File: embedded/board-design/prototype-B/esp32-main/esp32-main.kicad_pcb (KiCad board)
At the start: 2 copper layers, 75 x 135.5 mm, 84 parts, among them J1 Conn_ARM_JTAG_SWD_10, J2 Conn_01x08_Socket, J3 Conn_01x08_Socket, J4 0473460001, J5 Conn_01x02_Socket, J6 Conn_01x03_Socket, J7 Conn_01x02_Socket, J8 Conn_01x03_Socket, Q1 BC817, Q2 BC817, Q3 FDN340P, Q4 FDN340P, Q5 BC807, Q6 FDN340P, Q7 FDN340P, U1 ESP32-WROVER-E, U2 BD48ExxG, U3 FT231XS, U4 TPS61090, U5 LTC4054ES5-4.2

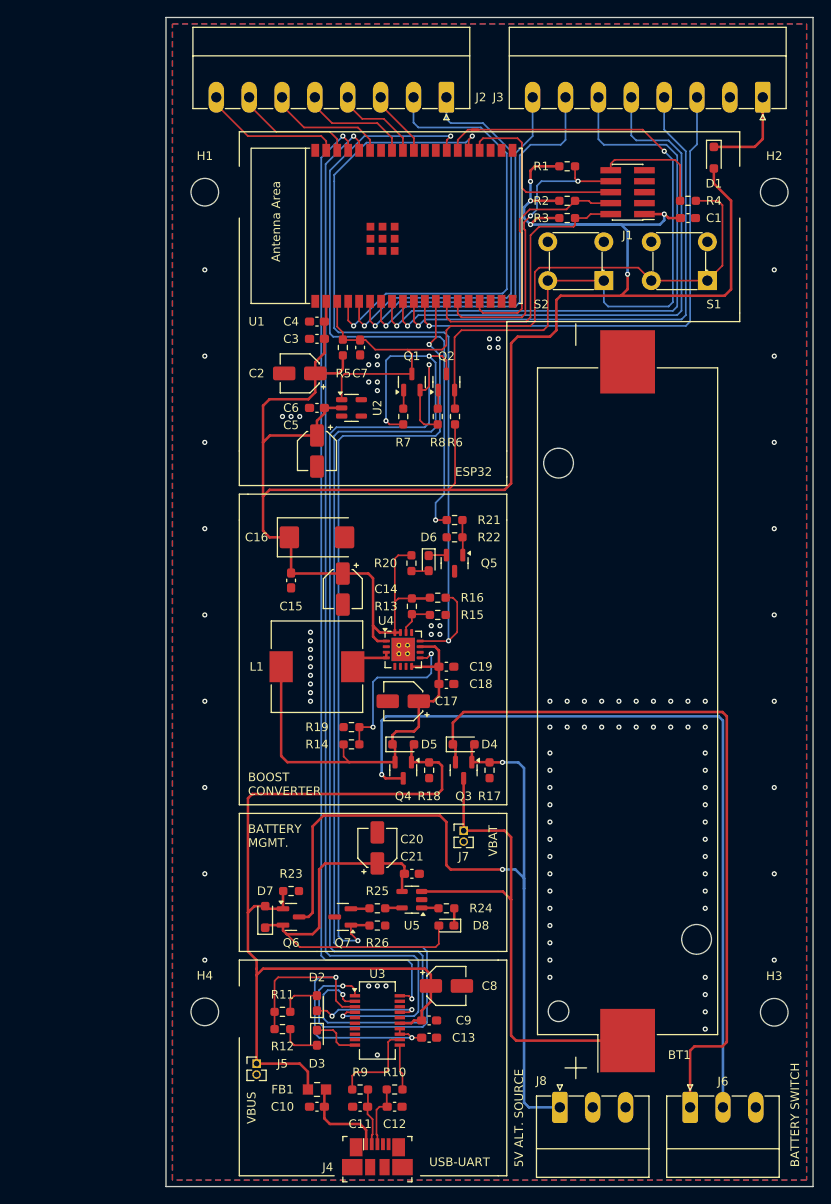
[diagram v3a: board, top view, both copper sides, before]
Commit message: [prototype-B]
Refactored hardware implementation. Reduced board size.

Signed-off-by: Nicolae-Andrei Vasile <vasilenicolaeandrei@gmail.com>
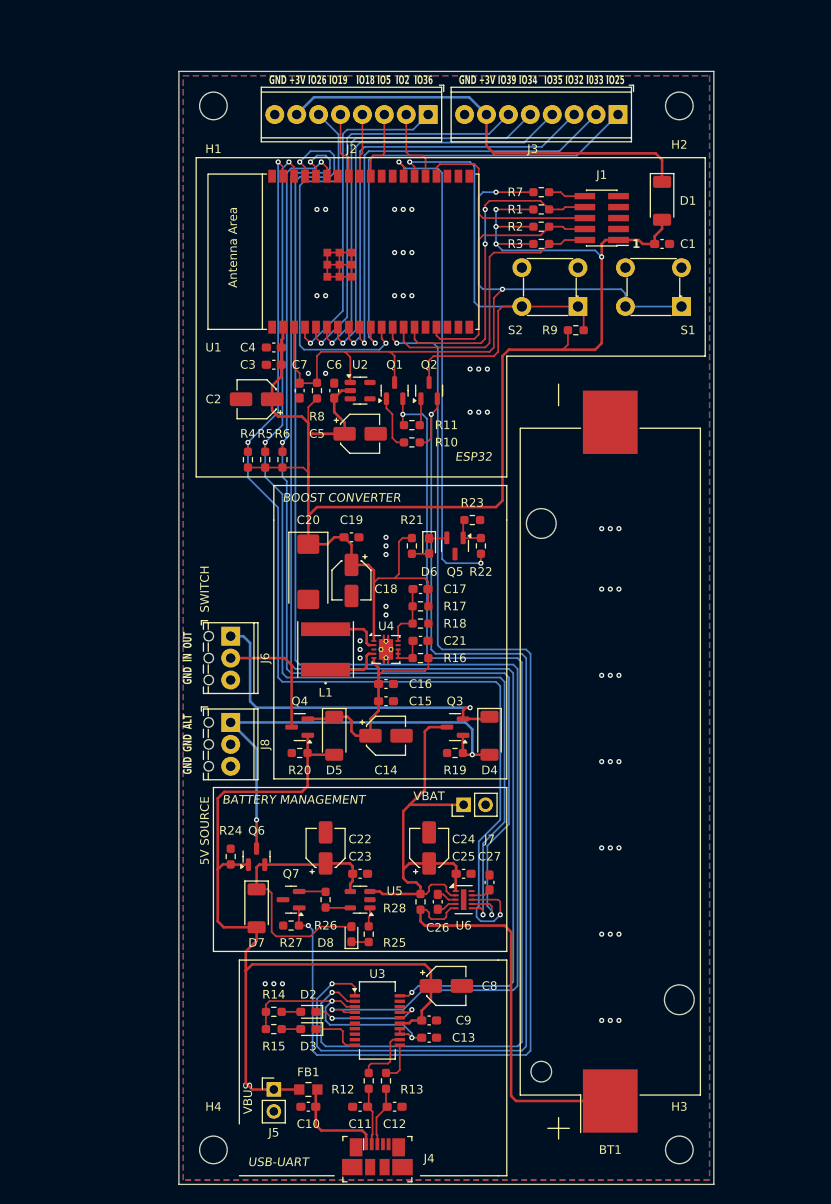
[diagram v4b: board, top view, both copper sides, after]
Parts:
- removed the R26 at (132.0, 126.0)
- added C22: 10uF/16V/20%/4x3mm, Capacitor_SMD:CP_Elec_4x3, F.Cu at (126.0, 117.0)
- added C23: 100nF/6.3V/20%/C0603, Capacitor_SMD:C_0603_1608Metric_Pad1.08x0.95mm_HandSolder, F.Cu at (130.0, 120.0)
- added C24: 10uF/16V/20%/4x3mm, Capacitor_SMD:CP_Elec_4x3, F.Cu at (138.0, 117.0)
- added C25: 100nF/6.3V/20%/C0603, Capacitor_SMD:C_0603_1608Metric_Pad1.08x0.95mm_HandSolder, F.Cu at (142.0, 120.0)
- added C26: 470nF/6.3V/20%/C0603, Capacitor_SMD:C_0603_1608Metric_Pad1.08x0.95mm_HandSolder, F.Cu at (139.0, 123.2)
- added C27: 1uF/6.3V/20%/C0603, Capacitor_SMD:C_0603_1608Metric_Pad1.08x0.95mm_HandSolder, F.Cu at (145.0, 121.0)
- added R27: 10K/R0603, Resistor_SMD:R_0603_1608Metric_Pad0.98x0.95mm_HandSolder, F.Cu at (122.0, 126.0)
- added R28: 50m/R0603, Resistor_SMD:R_0603_1608Metric_Pad0.98x0.95mm_HandSolder, F.Cu at (137.0, 123.2)
- added R4: 10K/R0603, Resistor_SMD:R_0603_1608Metric_Pad0.98x0.95mm_HandSolder, F.Cu at (117.0, 72.0)
- added U6: LTC2959, Package_DFN_QFN:DFN-10-1EP_2x3mm_P0.5mm_EP0.64x2.4mm, F.Cu at (142.0, 123.0)
- C16: value 220uF/16V/10%/D/Tantalum -> 100nF/6.3V/20%/C0603; footprint Capacitor_Tantalum_SMD:CP_EIA-7343-31_Kemet-D_Pad2.25x2.55mm_HandSolder -> Capacitor_SMD:C_0603_1608Metric_Pad1.08x0.95mm_HandSolder
- C17: value 22uF/16V/20%/4x3mm -> 2.2pF/6.3V/20%/C0603; footprint Capacitor_SMD:CP_Elec_4x3 -> Capacitor_SMD:C_0603_1608Metric_Pad1.08x0.95mm_HandSolder
- C18: value 10uF/6.3V/20%/C0603 -> 22uF/16V/20%/4x3mm; footprint Capacitor_SMD:C_0603_1608Metric_Pad1.08x0.95mm_HandSolder -> Capacitor_SMD:CP_Elec_4x3
- C19: value 100nF/6.3V/20%/C0603 -> 10uF/6.3V/20%/C0603
- C20: value 10uF/16V/20%/4x3mm -> 220uF/16V/10%/D/Tantalum; footprint Capacitor_SMD:CP_Elec_4x3 -> Capacitor_Tantalum_SMD:CP_EIA-7343-31_Kemet-D_Pad2.25x2.55mm_HandSolder
- D1, D4, D5, D7: value SMD22WS-TP -> PMEG3020EP; footprint Diode_SMD:D_SOD-323_HandSoldering -> Diode_SMD:D_SOD-128
- J2, J3: footprint Connector_Phoenix_MC:PhoenixContact_MC_1,5_8-G-3.81_1x08_P3.81mm_Horizontal -> TerminalBlock_Phoenix:TerminalBlock_Phoenix_MPT-0,5-8-2.54_1x08_P2.54mm_Horizontal
- J5, J7: footprint Connector_PinHeader_1.27mm:PinHeader_1x02_P1.27mm_Vertical -> Connector_PinHeader_2.54mm:PinHeader_1x02_P2.54mm_Vertical
- J6, J8: footprint Connector_Phoenix_MC:PhoenixContact_MC_1,5_3-G-3.81_1x03_P3.81mm_Horizontal -> TerminalBlock_Phoenix:TerminalBlock_Phoenix_MPT-0,5-3-2.54_1x03_P2.54mm_Horizontal
- L1: value CDRH103RNP-8R2NC-B -> NRS6010T1R5MMGF; footprint Inductor_SMD:L_10.4x10.4_H4.8 -> footprints:IND_TAIYO_NRS6010_TAY
- R1, R2, R3: value 100K/R0603 -> 10K/R0603
- R10: renamed from R9; value 27R/R0603 -> 10K/R0603
- R11: renamed from R10; value 27R/R0603 -> 10K/R0603
- R12: renamed from R11; value 270R/R0603 -> 27R/R0603
- R13: renamed from R12; value 270R/R0603 -> 27R/R0603
- R14: renamed from R13; value 1M/R0603 -> 270R/R0603
- R15: renamed from R14; value 2M/R0603 -> 270R/R0603
- R16: renamed from R15; value 180K/R0603 -> 100R/R0603
- R18: renamed from R17; value 100K/R0603 -> 180K/R0603
- R20: renamed from R19; value 390K/R0603 -> 100K/R0603
- R5: renamed from R4; value 0R(board mount) -> 10K/R0603
- R7: renamed from R6; value 10K/R0603 -> 0R(board mount)
- U4: value TPS61090 -> TPS63000; footprint Package_DFN_QFN:Texas_RSA_VQFN-16-1EP_4x4mm_P0.65mm_EP2.7x2.7mm_ThermalVias -> Package_SON:Texas_DRC0010J_ThermalVias
- moved R11 77.0 mm to (136.0, 68.0)
- moved J6 76.3 mm to (115.0, 92.5), turned to -90 degrees
- moved R10 75.2 mm to (136.0, 70.0)
- moved J8 58.7 mm to (115.0, 102.5), turned to -90 degrees
- moved R5 57.5 mm to (119.0, 72.0), turned to -90 degrees
- moved R14 49.6 mm to (120.0, 136.0), turned to 180 degrees
- moved R15 34.2 mm to (120.0, 138.0), turned to 180 degrees
- moved C20 33.0 mm to (124.0, 85.0), turned to -90 degrees
- moved R7 27.9 mm to (151.0, 41.0), turned to 180 degrees
- moved C21 27.0 mm to (137.0, 93.0)
- moved H3 19.4 mm to (167.0, 152.0)
- moved R9 18.9 mm to (155.0, 57.0), turned to 0 degrees
- moved C16 18.8 mm to (133.0, 98.0)
- moved R18 18.8 mm to (137.0, 91.0), turned to 180 degrees
- moved C19 18.6 mm to (129.0, 81.0)
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- renumbered R16 to R17, R18 to R19, R20 to R21, R21 to R22, R22 to R23, R23 to R24, R24 to R25, R25 to R26, R5 to R6, R7 to R8, R8 to R9
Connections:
- net /GPIO18/VSPICLK renamed /GPIO18
- net /GPIO19/VSPIQ renamed /GPIO19
- net /GPIO5/VSPICS0 renamed /GPIO5
- BT1 pad 1: VBAT -> Net-(BT1-+)
- C14 pad 1: +3V3 -> Net-(D5-K)
- C15 pad 1: +3V3 -> Net-(D5-K)
- C16 pad 1: +3V3 -> Net-(D5-K)
- C17 pad 1: Net-(D5-K) -> +3V3
- C17 pad 2: GND -> Net-(U4-FB)
- C18 pad 1: Net-(D5-K) -> +3V3
- C19 pad 1: Net-(D5-K) -> +3V3
- C20 pad 1: Net-(D7-K) -> +3V3
- C21 pad 1: Net-(D7-K) -> Net-(U4-EN)
- J2 pad 1: /GPIO39 -> /GPIO36
- J2 pad 2: /GPIO36 -> /GPIO2
- J2 pad 6: /GPIO21/VSPIHD -> /GPIO26
- J2 pad 7: /GPIO22/VSPIWP -> Net-(D1-K)
- J2 pad 8: /GPIO23/VSPID -> GND
- J3 pad 1: Net-(D1-K) -> /GPIO25
- J3 pad 2: GND -> /GPIO33
- J3 pad 3: /GPIO26 -> /GPIO32
- J3 pad 4: /GPIO25 -> /GPIO35
- J3 pad 5: /GPIO33 -> /GPIO34
- J3 pad 6: /GPIO32 -> /GPIO39
- J3 pad 7: /GPIO35 -> Net-(D1-K)
- J3 pad 8: /GPIO34 -> GND
- L1 pad 1: Net-(D5-K) -> Net-(U4-L1)
- L1 pad 2: Net-(L1-Pad2) -> Net-(U4-L2)
- Q2 pad 2: /BOOT -> /usb-uart/~{DTR}
- Q2 pad 3: /usb-uart/~{DTR} -> /BOOT
- R10 pad 1: Net-(U3-USBDM) -> Net-(Q1-B)
- R10 pad 2: /usb-uart/D- -> /usb-uart/~{DTR}
- R11 pad 1: Net-(U3-USBDP) -> Net-(Q2-B)
- R11 pad 2: /usb-uart/D+ -> /usb-uart/~{RTS}
- R12 pad 1: Net-(D2-A) -> Net-(U3-USBDM)
- R12 pad 2: Net-(U3-3V3OUT) -> /usb-uart/D-
- R13 pad 1: Net-(D3-A) -> Net-(U3-USBDP)
- R13 pad 2: Net-(U3-3V3OUT) -> /usb-uart/D+
- R14 pad 1: +3V3 -> Net-(D2-A)
- R14 pad 2: Net-(U4-FB) -> Net-(U3-3V3OUT)
- R15 pad 1: Net-(D5-K) -> Net-(D3-A)
- R15 pad 2: Net-(U4-LBI) -> Net-(U3-3V3OUT)
- R16 pad 1: Net-(U4-FB) -> Net-(U4-EN)
- R16 pad 2: GND -> Net-(D5-K)
- R17 pad 1: +3V3 -> Net-(U4-FB)
- R17 pad 2: /power-supply/LDO -> +3V3
- R18 pad 2: ALT -> Net-(U4-FB)
- R19 pad 2: VBUS -> ALT
- R20 pad 2: Net-(U4-LBI) -> VBUS
- R5 pad 1: Net-(J1-~{RESET}) -> /battery/SCL
- R5 pad 2: Net-(Q1-C) -> +3V3
- R6 pad 1: +3V3 -> /battery/SDA
- R6 pad 2: Net-(Q1-C) -> +3V3
- R7 pad 1: +3V3 -> Net-(J1-~{RESET})
- R7 pad 2: /BOOT -> Net-(Q1-C)
- R8 pad 1: Net-(Q1-B) -> +3V3
- R8 pad 2: /usb-uart/~{DTR} -> Net-(Q1-C)
- R9 pad 1: Net-(Q2-B) -> +3V3
- R9 pad 2: /usb-uart/~{RTS} -> /BOOT
- U1 pad 24: /power-supply/LDO -> /GPIO2
- U1 pad 33: /GPIO21/VSPIHD -> /battery/SDA
- U1 pad 36: /GPIO22/VSPIWP -> /battery/SCL
- U1 pad 37: /GPIO23/VSPID -> /battery/BAT_INT
- U3 pad 20: /U0TXD -> /U0RXD
- U3 pad 4: /U0RXD -> /U0TXD
- U4 pad 10: GND -> Net-(U4-FB)
- U4 pad 11: Net-(D5-K) -> GND
- U4 pad 2: unconnected-(U4-NC-Pad2) -> Net-(U4-L2)
- U4 pad 3: Net-(L1-Pad2) -> GND
- U4 pad 4: Net-(L1-Pad2) -> Net-(U4-L1)
- U4 pad 5: GND -> Net-(D5-K)
- U4 pad 6: GND -> Net-(U4-EN)
- U4 pad 7: GND -> Net-(U4-EN)
- U4 pad 8: Net-(D5-K) -> Net-(U4-EN)
- U4 pad 9: Net-(U4-LBI) -> GND
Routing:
- net /battery/BAT_INT: track 0.00 -> 127.9 mm, vias 0 -> 3
- net /battery/SDA: track 0.00 -> 123.8 mm, vias 0 -> 3
- net /battery/SCL: track 0.00 -> 120.3 mm, vias 0 -> 3
- net /power-supply/LDO: track 96.1 -> 0.00 mm, vias 2 -> 0
- net Net-(J6-Pin_2): track 93.7 -> 14.6 mm, vias 1 -> 0
- net +3V3: track 245.0 -> 190.9 mm, vias 5 -> 4
- net /battery/SHDN: track 92.4 -> 142.2 mm
- net Net-(BT1-+): track 0.00 -> 48.7 mm
- net Net-(D4-K): track 86.1 -> 40.2 mm, vias 0 -> 1
- net ALT: track 95.6 -> 52.4 mm
- net /U0TXD: track 114.4 -> 157.4 mm
- net Net-(D1-K): track 10.9 -> 50.9 mm
- net /BOOT: track 88.6 -> 59.3 mm
- net Net-(D5-K): track 49.2 -> 25.9 mm
- net Net-(U4-LBI): track 19.7 -> 0.00 mm, vias 2 -> 0
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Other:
- board size 75 x 135.5 mm -> 62 x 129 mm
- board text added: "1"
- board text added: "5V SOURCE"
- board text added: "BATTERY MANAGEMENT"
- board text added: "GND +3V IO26 IO19"
- board text added: "GND +3V IO39 IO34"
- board text added: "GND GND ALT"
- board text added: "GND IN OUT"
- board text added: "IO18 IO5 IO2 IO36"
- board text added: "IO35 IO32 I033 IO25"
- board text added: "SWITCH"
- board text removed: "5V ALT. SOURCE"
- board text removed: "BATTERY MGMT."
- board text removed: "BATTERY SWITCH"
